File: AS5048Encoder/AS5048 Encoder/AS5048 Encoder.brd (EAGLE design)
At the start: 50 x 50 mm, 18 parts

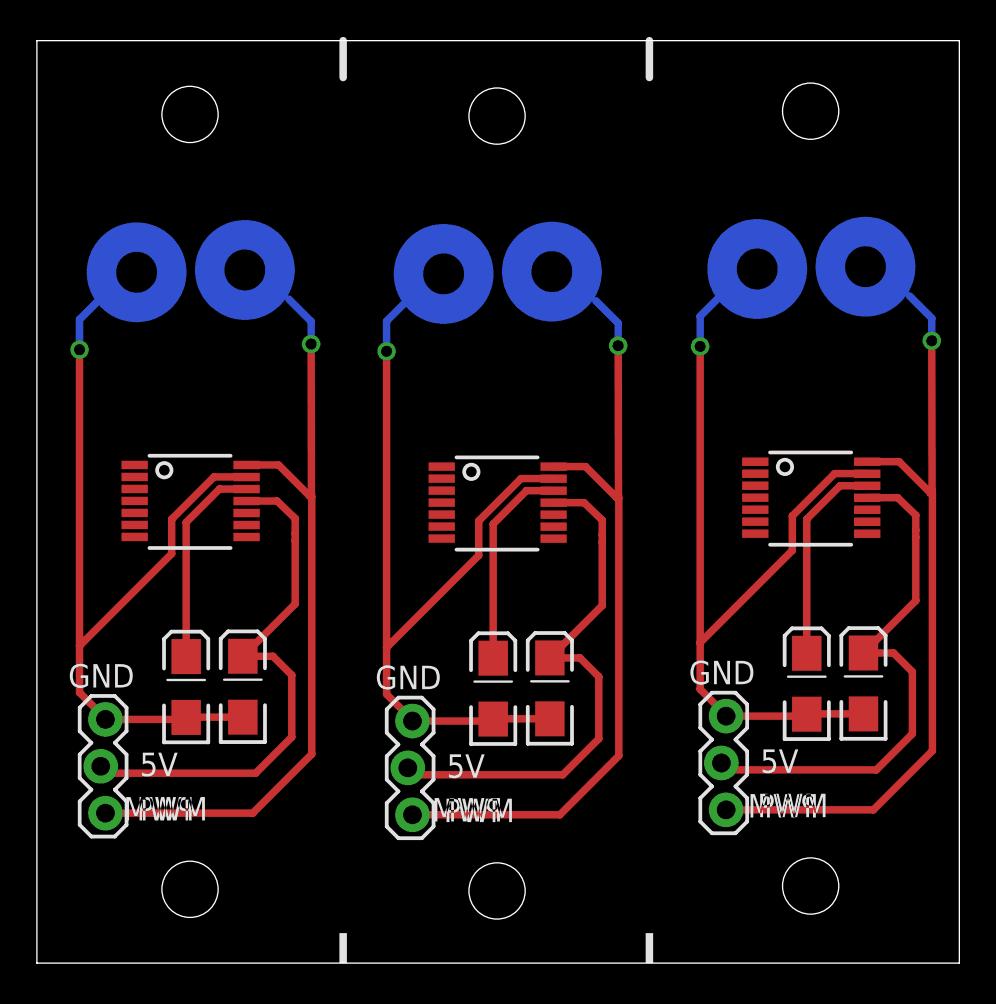
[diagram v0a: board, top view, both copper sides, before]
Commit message: added ethernet jack to docs
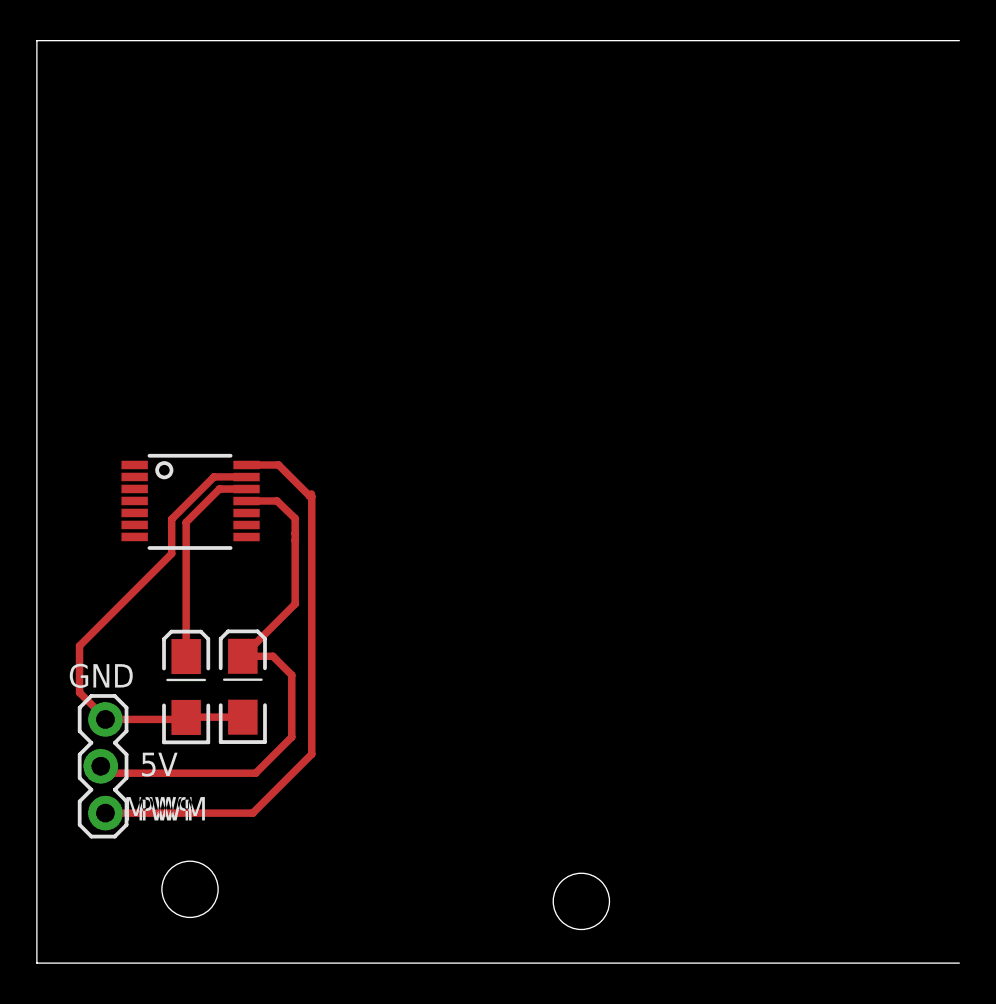
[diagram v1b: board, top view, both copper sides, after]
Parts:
- removed C1, C5: 100nF, SparkFun-Passives:EIA3216-KIT
- removed C2, C6: 10uF, SparkFun-Passives:EIA3216-KIT
- removed JP2, JP3: (no value), SparkFun-Connectors:1X03_LOCK
- removed U$4, U$7: AS5048, austriamicrosystems:TSOP14
- removed U$5, U$6, U$8, U$9: (no value), SparkFun-Electromechanical:STAND-OFF-TIGHT
- moved U$2 47.6 mm to (29.5, 3.35)
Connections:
- removed net 3V1: C2.A, U$4.12
- removed net 3V2: C6.A, U$7.12
- removed net GND1: C1.C, C2.C, JP2.1, U$4.13
- removed net GND2: C5.C, C6.C, JP3.1, U$7.13
- removed net PWM1: JP2.3, U$4.14
- removed net PWM2: JP3.3, U$7.14
- removed net VCC1: C1.A, JP2.2, U$4.11
- removed net VCC2: C5.A, JP3.2, U$7.11
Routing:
- net GND2: track 46.3 -> 0.00 mm, vias 1 -> 0
- net GND1: track 46.3 -> 0.00 mm, vias 1 -> 0
- net PWM2: track 42.0 -> 0.00 mm, vias 1 -> 0
- net PWM1: track 42.0 -> 0.00 mm, vias 1 -> 0
- net VCC1: track 29.4 -> 0.00 mm
- net VCC2: track 29.4 -> 0.00 mm
- net GND: track 46.3 -> 26.1 mm, vias 1 -> 0
- net 3V2: track 11.3 -> 0.00 mm
- net 3V1: track 11.3 -> 0.00 mm
- net PWM: track 42.0 -> 30.9 mm, vias 1 -> 0
